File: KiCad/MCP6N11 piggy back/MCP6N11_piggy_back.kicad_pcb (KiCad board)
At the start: 2 copper layers, 22.5 x 14.5 mm, 19 parts, among them J1 Conn_01x02_Male, J2 Conn_01x01_Male, J4 Conn_01x02_Male, J5 Conn_01x02_Male, U1 MCP6N11

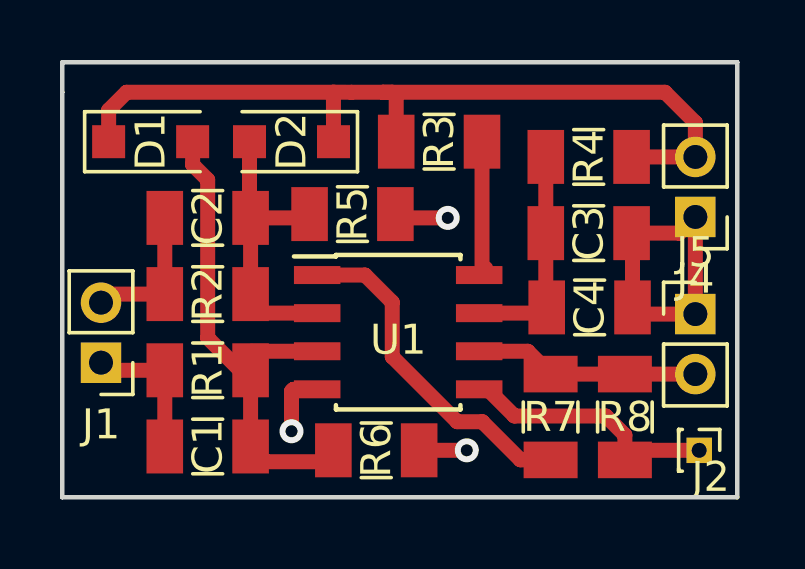
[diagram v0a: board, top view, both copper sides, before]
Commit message: fault in schemtic regarding Rf and Rg
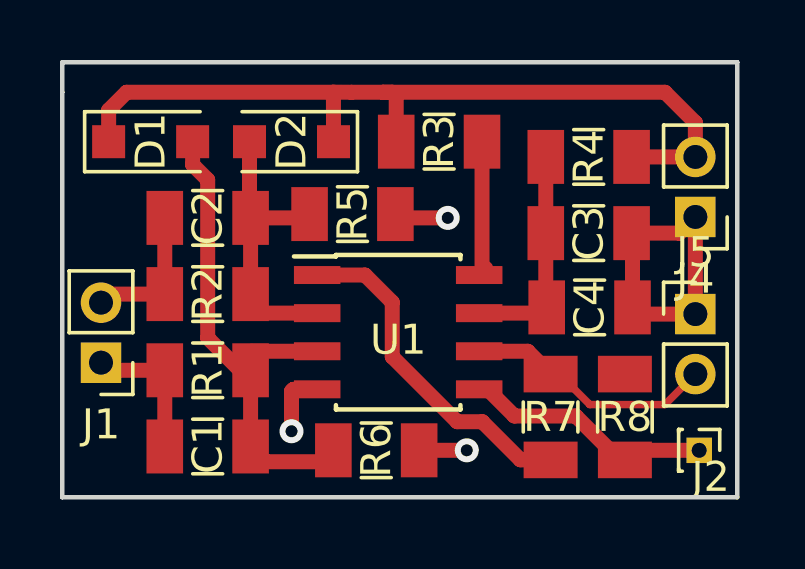
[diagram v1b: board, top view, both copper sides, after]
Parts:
- R1, R2: value 4k99 -> 9k10
- R8: value 1k -> 100k
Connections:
- R8 pad 2: Net-(J5-Pad2) -> Net-(R7-Pad1)
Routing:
- net Net-(J5-Pad2): track 7.52 -> 8.36 mm
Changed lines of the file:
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@@
-(kicad_pcb (version 20171130) (host pcbnew "(5.0.0-rc2-dev-444-g2974a2c10)")
+(kicad_pcb (version 20171130) (host pcbnew "(5.0.0-rc2-dev-451-g0294e41cb)")
   (general
     (thickness 1.6)
     (drawings 5)
-    (tracks 80)
+    (tracks 82)
     (zones 0)
     (modules 19)
@@
       (effects (font (size 1 1) (thickness 0.15)))
     )
-    (fp_text value 4k99 (at 0 1.85 180) (layer F.Fab)
+    (fp_text value 9k10 (at 0 1.85 180) (layer F.Fab)
       (effects (font (size 1 1) (thickness 0.15)))
     )
@@
       (effects (font (size 1 1) (thickness 0.15)))
     )
-    (fp_text value 4k99 (at 0 1.85 180) (layer F.Fab)
+    (fp_text value 9k10 (at 0 1.85 180) (layer F.Fab)
       (effects (font (size 1 1) (thickness 0.15)))
     )
@@
       (effects (font (size 1 1) (thickness 0.15)))
     )
-    (fp_text value 1k (at 0 1.85 90) (layer F.Fab)
+    (fp_text value 100k (at 0 1.85 90) (layer F.Fab)
       (effects (font (size 1 1) (thickness 0.15)))
     )
@@
     (fp_line (start -1.6 0.8) (end -1.6 -0.8) (layer F.Fab) (width 0.1))
     (pad 2 smd rect (at 1.43 0 90) (size 1.22 1.8) (layers F.Cu F.Paste F.Mask)
-      (net 9 "Net-(J5-Pad2)"))
+      (net 10 "Net-(R7-Pad1)"))
     (pad 1 smd rect (at -1.43 0 90) (size 1.22 1.8) (layers F.Cu F.Paste F.Mask)
       (net 8 "Net-(J2-Pad1)"))
@@
   (segment (start 132.591 103) (end 133.604 104.013) (width 0.5) (layer F.Cu) (net 7))
   (segment (start 131.478 105.156) (end 133.604 105.156) (width 0.5) (layer F.Cu) (net 7))
-  (segment (start 131.2545 114.427) (end 131.2545 115.255) (width 0.5) (layer F.Cu) (net 8))
-  (segment (start 130.6195 113.792) (end 131.2545 114.427) (width 0.5) (layer F.Cu) (net 8))
-  (segment (start 127.5715 113.792) (end 130.6195 113.792) (width 0.5) (layer F.Cu) (net 8))
+  (segment (start 131.5745 114.935) (end 133.731 114.935) (width 0.5) (layer F.Cu) (net 8))
+  (segment (start 131.2545 115.255) (end 131.5745 114.935) (width 0.5) (layer F.Cu) (net 8))
+  (segment (start 131.0792 115.255) (end 131.2545 115.255) (width 0.5) (layer F.Cu) (net 8))
+  (segment (start 129.6162 113.792) (end 131.0792 115.255) (width 0.5) (layer F.Cu) (net 8))
+  (segment (start 127.5715 113.792) (end 129.6162 113.792) (width 0.5) (layer F.Cu) (net 8))
   (segment (start 126.398 112.903) (end 126.6825 112.903) (width 0.5) (layer F.Cu) (net 8))
   (segment (start 126.6825 112.903) (end 127.5715 113.792) (width 0.5) (layer F.Cu) (net 8))
-  (segment (start 131.5745 114.935) (end 133.731 114.935) (width 0.5) (layer F.Cu) (net 8))
-  (segment (start 131.2545 115.255) (end 131.5745 114.935) (width 0.5) (layer F.Cu) (net 8))
+  (segment (start 126.398 111.633) (end 128.016 111.633) (width 0.5) (layer F.Cu) (net 9))
   (segment (start 128.016 111.633) (end 128.778 112.395) (width 0.5) (layer F.Cu) (net 9))
-  (segment (start 126.398 111.633) (end 128.016 111.633) (width 0.5) (layer F.Cu) (net 9))
-  (segment (start 131.2545 112.395) (end 128.778 112.395) (width 0.5) (layer F.Cu) (net 9))
-  (segment (start 133.604 112.395) (end 131.2545 112.395) (width 0.5) (layer F.Cu) (net 9))
+  (segment (start 129.068 112.395) (end 128.778 112.395) (width 0.25) (layer F.Cu) (net 9))
+  (segment (start 130.084 113.411) (end 129.068 112.395) (width 0.25) (layer F.Cu) (net 9))
+  (segment (start 132.588 113.411) (end 130.084 113.411) (width 0.25) (layer F.Cu) (net 9))
+  (segment (start 133.604 112.395) (end 132.588 113.411) (width 0.25) (layer F.Cu) (net 9))
+  (segment (start 125.6665 113.9825) (end 126.502502 113.9825) (width 0.5) (layer F.Cu) (net 10))
+  (segment (start 127.772502 115.2525) (end 128.778 115.2525) (width 0.5) (layer F.Cu) (net 10))
+  (segment (start 123.5 111.816) (end 125.6665 113.9825) (width 0.5) (layer F.Cu) (net 10))
   (segment (start 128.778 115.2525) (end 128.778 115.255) (width 0.5) (layer F.Cu) (net 10))
-  (segment (start 127.772502 115.2525) (end 128.778 115.2525) (width 0.5) (layer F.Cu) (net 10))
+  (segment (start 123.5 110) (end 123.5 111.816) (width 0.5) (layer F.Cu) (net 10))
+  (segment (start 126.502502 113.9825) (end 127.772502 115.2525) (width 0.5) (layer F.Cu) (net 10))
   (segment (start 120.998 109.093) (end 122.593 109.093) (width 0.5) (layer F.Cu) (net 10))
-  (segment (start 123.5 110) (end 123.5 111.816) (width 0.5) (layer F.Cu) (net 10))
   (segment (start 122.593 109.093) (end 123.5 110) (width 0.5) (layer F.Cu) (net 10))
-  (segment (start 123.5 111.816) (end 125.6665 113.9825) (width 0.5) (layer F.Cu) (net 10))
-  (segment (start 125.6665 113.9825) (end 126.502502 113.9825) (width 0.5) (layer F.Cu) (net 10))
-  (segment (start 126.502502 113.9825) (end 127.772502 115.2525) (width 0.5) (layer F.Cu) (net 10))
   (segment (start 126.398 109.093) (end 126.619 108.872) (width 0.5) (layer F.Cu) (net 11))
   (segment (start 126.492 108.999) (end 126.398 109.093) (width 0.5) (layer F.Cu) (net 11))
